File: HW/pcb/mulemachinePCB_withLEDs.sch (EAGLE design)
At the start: 31 parts, among them IC1 LD117AV50, IC2 MEGA8-P, J1 DCJ0202, Q1 16Mhz

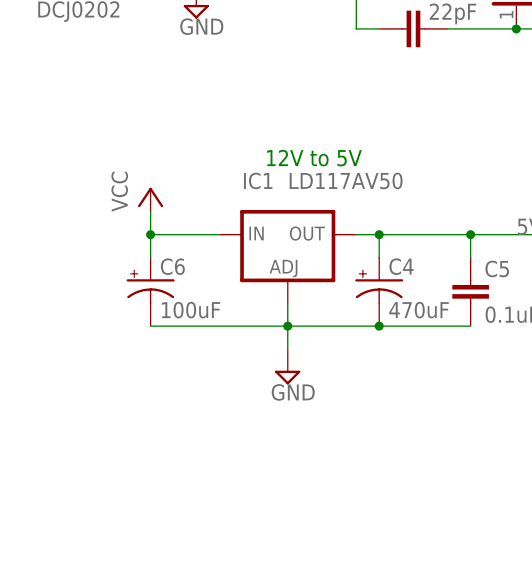
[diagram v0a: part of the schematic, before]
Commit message: changed 12V side cap C6 to 470uF. rerouted board
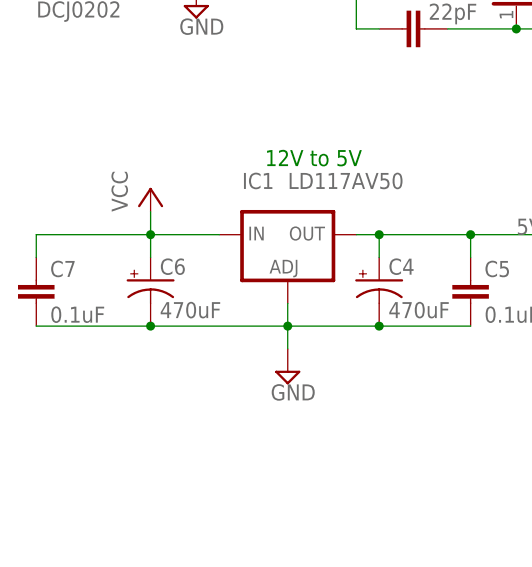
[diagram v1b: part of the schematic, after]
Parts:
- added C7: 0.1uF, capacitor-wima:C2,5-3
- C6: value 100uF -> 470uF
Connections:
- net GND: now also C7.2
- net VCC: now also C7.1
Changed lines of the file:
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@@
 <part name="T3" library="transistor-neu-to92" library_urn="urn:adsk.eagle:library:397" deviceset="*-NPN-" device="TO92-EBC" package3d_urn="urn:adsk.eagle:package:28763/2" technology="2N4401"/>
 <part name="C5" library="capacitor-wima" library_urn="urn:adsk.eagle:library:116" deviceset="C" device="2,5-3" package3d_urn="urn:adsk.eagle:package:5436/1" value="0.1uF"/>
-<part name="C6" library="rcl" library_urn="urn:adsk.eagle:library:334" deviceset="CPOL-US" device="E2.5-6" package3d_urn="urn:adsk.eagle:package:23349/1" value="100uF"/>
+<part name="C6" library="rcl" library_urn="urn:adsk.eagle:library:334" deviceset="CPOL-US" device="E2.5-6" package3d_urn="urn:adsk.eagle:package:23349/1" value="470uF"/>
 <part name="S2" library="switch-omron" library_urn="urn:adsk.eagle:library:377" deviceset="10-XX" device="" package3d_urn="urn:adsk.eagle:package:27496/1"/>
+<part name="C7" library="capacitor-wima" library_urn="urn:adsk.eagle:library:116" deviceset="C" device="2,5-3" package3d_urn="urn:adsk.eagle:package:5436/1" value="0.1uF"/>
 </parts>
 <sheets>
@@
 <attribute name="VALUE" x="71.755" y="6.35" size="1.778" layer="96"/>
 </instance>
+<instance part="C7" gate="G$1" x="-38.1" y="30.48" smashed="yes">
+<attribute name="NAME" x="-36.576" y="30.861" size="1.778" layer="95"/>
+<attribute name="VALUE" x="-36.576" y="25.781" size="1.778" layer="96"/>
+</instance>
 </instances>
 <busses>
@@
 <wire x1="-25.4" y1="33.02" x2="-25.4" y2="35.56" width="0.1524" layer="91"/>
 <junction x="-25.4" y="35.56"/>
+<wire x1="-25.4" y1="35.56" x2="-38.1" y2="35.56" width="0.1524" layer="91"/>
+<pinref part="C7" gate="G$1" pin="1"/>
+<wire x1="-38.1" y1="35.56" x2="-38.1" y2="33.02" width="0.1524" layer="91"/>
 </segment>
 <segment>
@@
 <pinref part="C6" gate="G$1" pin="-"/>
 <wire x1="-25.4" y1="25.4" x2="-10.16" y2="25.4" width="0.1524" layer="91"/>
-</segment>
-<segment>
+<pinref part="C7" gate="G$1" pin="2"/>
+<wire x1="-25.4" y1="25.4" x2="-38.1" y2="25.4" width="0.1524" layer="91"/>
+<junction x="-25.4" y="25.4"/>
+</segment>
+<segment>

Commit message: added decoupling cap for MCU to schematic. organized schematic with groups
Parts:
- added C8: 0.1uF, capacitor-wima:C2,5-3
- R1, R2, R3: value 150 -> 150R
- R4, R5, R6: value 200 -> 200R
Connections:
- net GREENLED renamed LED_GREEN
- net N$1 renamed PUMP_VODKA
- net N$22 renamed PUMP_GB
- net N$23 renamed PUMP_LIME
- net ORANGELED renamed LED_ORANGE
- net P1 renamed PUMP_VODKA_VCC
- net P2 renamed PUMP_GB_VCC
- net P3 renamed PUMP_LIME_VCC
- net YELLOWLED renamed LED_YELLOW
- net 5V: now also C8.2
- net GND: now also C8.1
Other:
- note removed: "12V to 5V"
- note removed: "DEBUG INTERFACE"
- note removed: "Manual Override Button"
- note removed: "Pump Control"
- note removed: "Strength Tuner"
- note removed: "Sweetness Tuner"
- note removed: "USER INTERFACE"
- moved on the sheet: C1, C2, C3, C4, C5, C6, C7, D1, D2, D3, IC1, IC2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

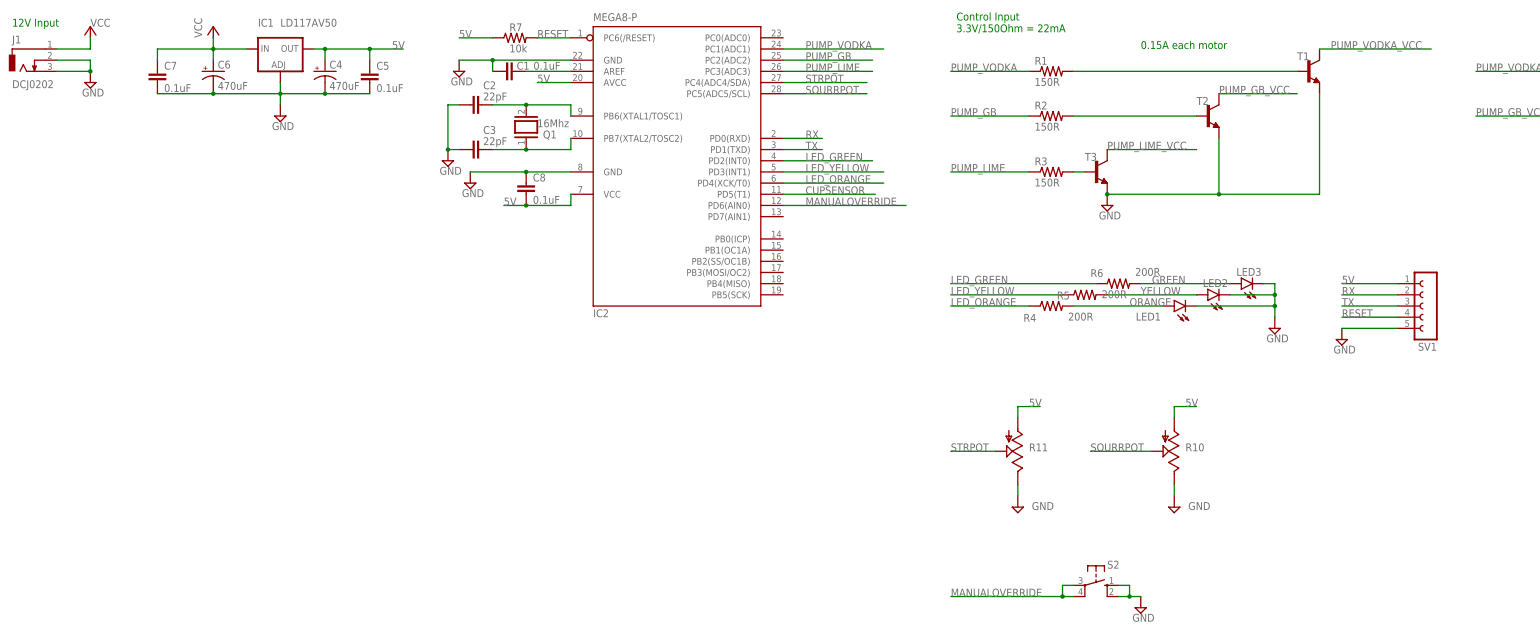
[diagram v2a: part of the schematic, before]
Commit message: rotated MCU to allow for better routing. added top and bottom layer ground planes with vias connecting them.
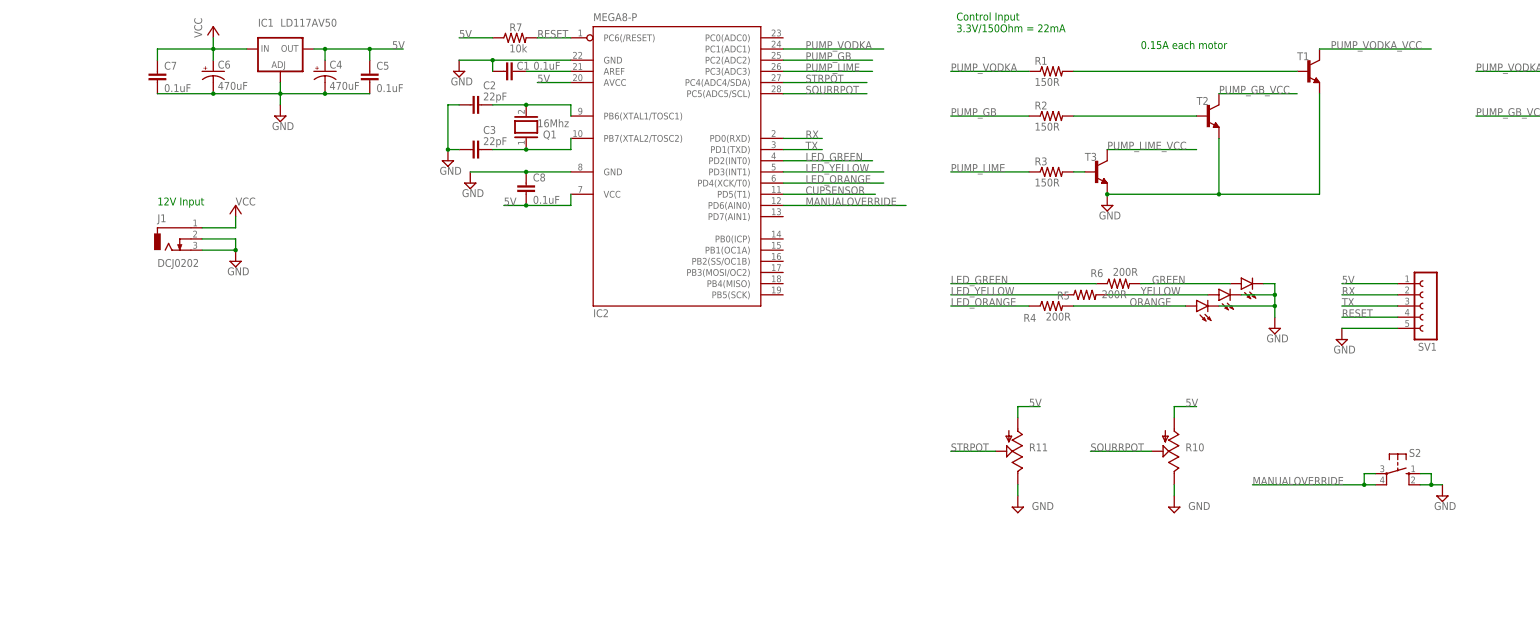
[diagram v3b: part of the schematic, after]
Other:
- moved on the sheet: J1, S2

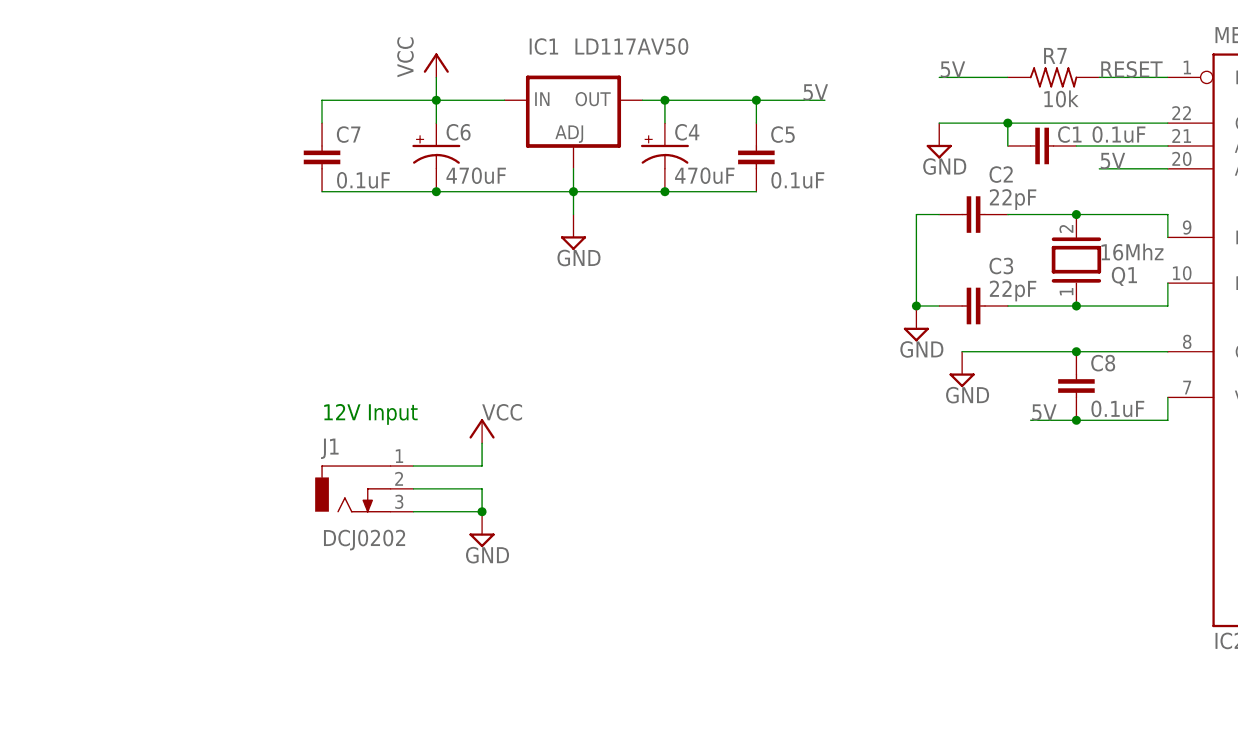
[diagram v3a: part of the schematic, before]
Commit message: adjusted net classes so that pump VCCs lines were also considered power traces (wider). rerouted and adjusted GND planes
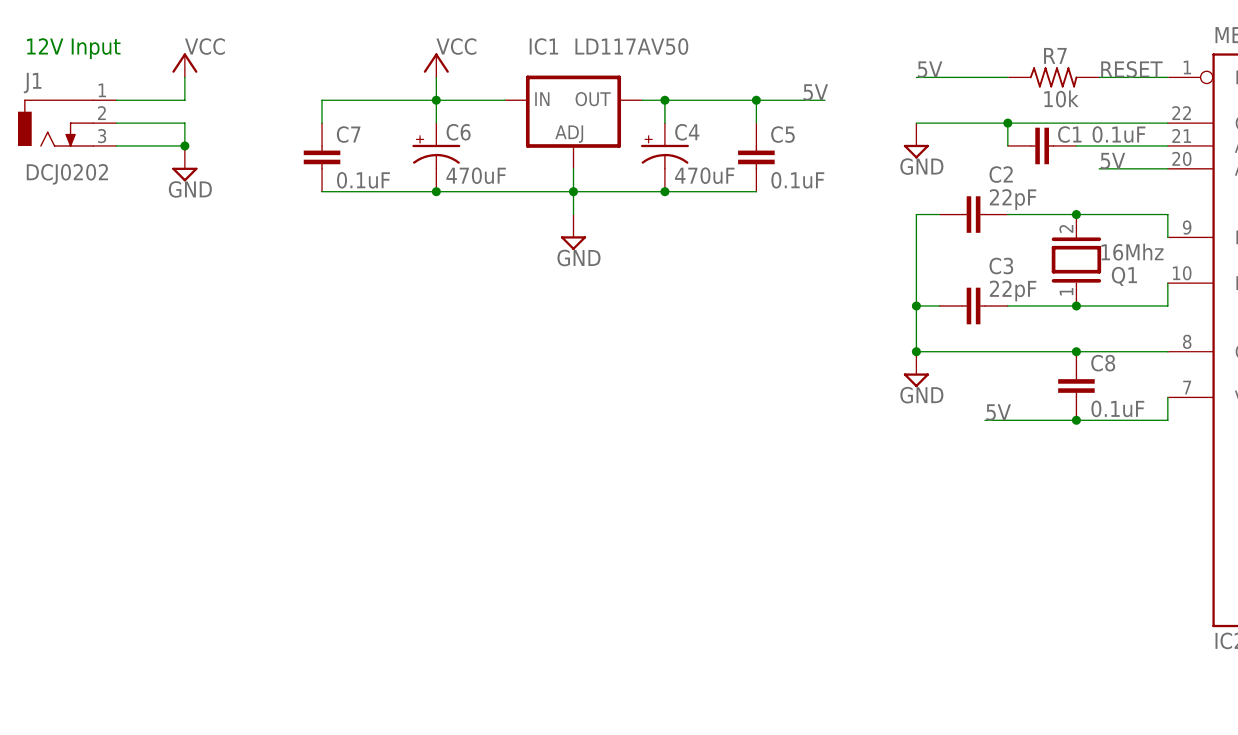
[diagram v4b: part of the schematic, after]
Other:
- moved on the sheet: J1
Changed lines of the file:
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@@
 <part name="C7" library="capacitor-wima" library_urn="urn:adsk.eagle:library:116" deviceset="C" device="2,5-3" package3d_urn="urn:adsk.eagle:package:5436/1" value="0.1uF"/>
 <part name="C8" library="capacitor-wima" library_urn="urn:adsk.eagle:library:116" deviceset="C" device="2,5-3" package3d_urn="urn:adsk.eagle:package:5436/1" value="0.1uF"/>
-<part name="SUPPLY12" library="supply2" library_urn="urn:adsk.eagle:library:372" deviceset="GND" device=""/>
 </parts>
 <sheets>
 <sheet>
 <plain>
-<text x="-68.58" y="73.66" size="1.778" layer="91" grouprefs="12VCONNECTOR">12V Input</text>
+<text x="-101.6" y="114.3" size="1.778" layer="91" grouprefs="12VCONNECTOR">12V Input</text>
 <text x="274.32" y="114.3" size="1.778" layer="91" grouprefs="PUMP_CONNECTOR">Harness</text>
 <text x="154.94" y="109.22" size="1.778" layer="91" grouprefs="PUMP_DRIVERS">0.15A each motor</text>
@@
 <attribute name="VALUE" x="-40.64" y="114.3" size="1.778" layer="96"/>
 </instance>
-<instance part="SUPPLY3" gate="GND" x="-50.8" y="60.96" smashed="yes" grouprefs="12VCONNECTOR">
-<attribute name="VALUE" x="-52.705" y="57.785" size="1.778" layer="96"/>
-</instance>
-<instance part="P+2" gate="VCC" x="-50.8" y="73.66" smashed="yes" grouprefs="12VCONNECTOR">
-<attribute name="VALUE" x="-50.8" y="73.66" size="1.778" layer="96"/>
-</instance>
-<instance part="J1" gate="G$1" x="-66.04" y="66.04" smashed="yes" grouprefs="12VCONNECTOR">
-<attribute name="NAME" x="-68.58" y="69.85" size="1.778" layer="95"/>
-<attribute name="VALUE" x="-68.58" y="59.69" size="1.778" layer="96"/>
+<instance part="SUPPLY3" gate="GND" x="-83.82" y="101.6" smashed="yes" grouprefs="12VCONNECTOR">
+<attribute name="VALUE" x="-85.725" y="98.425" size="1.778" layer="96"/>
+</instance>
+<instance part="P+2" gate="VCC" x="-83.82" y="114.3" smashed="yes" grouprefs="12VCONNECTOR">
+<attribute name="VALUE" x="-83.82" y="114.3" size="1.778" layer="96"/>
+</instance>
+<instance part="J1" gate="G$1" x="-99.06" y="106.68" smashed="yes" grouprefs="12VCONNECTOR">
+<attribute name="NAME" x="-101.6" y="110.49" size="1.778" layer="95"/>
+<attribute name="VALUE" x="-101.6" y="100.33" size="1.778" layer="96"/>
 </instance>
 <instance part="X2" gate="G$1" x="279.4" y="101.6" smashed="yes" grouprefs="PUMP_CONNECTOR">
@@
 </instance>
 <instance part="P+3" gate="VCC" x="-55.88" y="114.3" smashed="yes" grouprefs="12VTO5V">
-<attribute name="VALUE" x="-58.42" y="111.76" size="1.778" layer="96" rot="R90"/>
+<attribute name="VALUE" x="-55.88" y="114.3" size="1.778" layer="96"/>
 </instance>
 <instance part="SUPPLY6" gate="GND" x="147.32" y="73.66" smashed="yes" grouprefs="PUMP_DRIVERS">
@@
 <attribute name="VALUE" x="11.43" y="108.458" size="1.778" layer="96"/>
 </instance>
-<instance part="SUPPLY1" gate="GND" x="0" y="104.14" smashed="yes" grouprefs="MCU">
-<attribute name="VALUE" x="-1.905" y="100.965" size="1.778" layer="96"/>
+<instance part="SUPPLY1" gate="GND" x="-2.54" y="104.14" smashed="yes" grouprefs="MCU">
+<attribute name="VALUE" x="-4.445" y="100.965" size="1.778" layer="96"/>
 </instance>
 <instance part="LED1" gate="G$1" x="167.64" y="50.8" smashed="yes" rot="R90" grouprefs="USER_INTERFACE">
@@
 <attribute name="NAME" x="129.54" y="17.78" size="1.778" layer="95"/>
 </instance>
-<instance part="SUPPLY11" gate="GND" x="2.54" y="78.74" smashed="yes" grouprefs="MCU">
-<attribute name="VALUE" x="0.635" y="75.565" size="1.778" layer="96"/>
+<instance part="SUPPLY11" gate="GND" x="-2.54" y="78.74" smashed="yes" grouprefs="MCU">
+<attribute name="VALUE" x="-4.445" y="75.565" size="1.778" layer="96"/>
 </instance>
 <instance part="C1" gate="G$1" x="12.7" y="104.14" smashed="yes" rot="R270" grouprefs="MCU">
@@
 <attribute name="NAME" x="16.764" y="79.121" size="1.778" layer="95"/>
 <attribute name="VALUE" x="16.764" y="74.041" size="1.778" layer="96"/>
-</instance>
-<instance part="SUPPLY12" gate="GND" x="-2.54" y="83.82" smashed="yes" grouprefs="MCU">
-<attribute name="VALUE" x="-4.445" y="80.645" size="1.778" layer="96"/>
 </instance>
 </instances>
@@
 <pinref part="J1" gate="G$1" pin="1"/>
 <pinref part="P+2" gate="VCC" pin="VCC"/>
-<wire x1="-58.42" y1="68.58" x2="-50.8" y2="68.58" width="0.1524" layer="91" grouprefs="12VCONNECTOR"/>
-<wire x1="-50.8" y1="68.58" x2="-50.8" y2="71.12" width="0.1524" layer="91" grouprefs="12VCONNECTOR"/>
+<wire x1="-91.44" y1="109.22" x2="-83.82" y2="109.22" width="0.1524" layer="91" grouprefs="12VCONNECTOR"/>
+<wire x1="-83.82" y1="109.22" x2="-83.82" y2="111.76" width="0.1524" layer="91" grouprefs="12VCONNECTOR"/>
 </segment>
 <segment>
@@
 </segment>
 </net>
-<net name="GND" class="0">
-<segment>
-<pinref part="C2" gate="G$1" pin="2"/>
-<wire x1="-2.54" y1="96.52" x2="0" y2="96.52" width="0.1524" layer="91" grouprefs="MCU"/>
-<pinref part="C3" gate="G$1" pin="2"/>
-<wire x1="0" y1="86.36" x2="-2.54" y2="86.36" width="0.1524" layer="91" grouprefs="MCU"/>
-<wire x1="-2.54" y1="86.36" x2="-2.54" y2="96.52" width="0.1524" layer="91" grouprefs="MCU"/>
-<pinref part="SUPPLY12" gate="GND" pin="GND"/>
-<junction x="-2.54" y="86.36" grouprefs="MCU"/>
-</segment>
+<net name="GND" class="1">
 <segment>
 <pinref part="SUPPLY3" gate="GND" pin="GND"/>
 <pinref part="J1" gate="G$1" pin="2"/>
-<wire x1="-58.42" y1="66.04" x2="-50.8" y2="66.04" width="0.1524" layer="91" grouprefs="12VCONNECTOR"/>
-<wire x1="-50.8" y1="66.04" x2="-50.8" y2="63.5" width="0.1524" layer="91" grouprefs="12VCONNECTOR"/>
-<junction x="-50.8" y="63.5" grouprefs="12VCONNECTOR"/>
+<wire x1="-91.44" y1="106.68" x2="-83.82" y2="106.68" width="0.1524" layer="91" grouprefs="12VCONNECTOR"/>
+<wire x1="-83.82" y1="106.68" x2="-83.82" y2="104.14" width="0.1524" layer="91" grouprefs="12VCONNECTOR"/>
+<junction x="-83.82" y="104.14" grouprefs="12VCONNECTOR"/>
 <pinref part="J1" gate="G$1" pin="3"/>
-<wire x1="-58.42" y1="63.5" x2="-50.8" y2="63.5" width="0.1524" layer="91" grouprefs="12VCONNECTOR"/>
+<wire x1="-91.44" y1="104.14" x2="-83.82" y2="104.14" width="0.1524" layer="91" grouprefs="12VCONNECTOR"/>
 </segment>
 <segment>
@@
 <segment>
 <pinref part="IC2" gate="G$1" pin="GND"/>
-<wire x1="0" y1="106.68" x2="7.62" y2="106.68" width="0.1524" layer="91" grouprefs="MCU"/>
+<wire x1="-2.54" y1="106.68" x2="7.62" y2="106.68" width="0.1524" layer="91" grouprefs="MCU"/>
 <pinref part="SUPPLY1" gate="GND" pin="GND"/>
 <pinref part="C1" gate="G$1" pin="2"/>
@@
 <pinref part="SUPPLY11" gate="GND" pin="GND"/>
 <pinref part="IC2" gate="G$1" pin="GND@1"/>
-<wire x1="2.54" y1="81.28" x2="15.24" y2="81.28" width="0.1524" layer="91" grouprefs="MCU"/>
+<wire x1="-2.54" y1="81.28" x2="15.24" y2="81.28" width="0.1524" layer="91" grouprefs="MCU"/>
 <pinref part="C8" gate="G$1" pin="1"/>
 <wire x1="15.24" y1="81.28" x2="25.4" y2="81.28" width="0.1524" layer="91" grouprefs="MCU"/>
 <junction x="15.24" y="81.28" grouprefs="MCU"/>
+<pinref part="C2" gate="G$1" pin="2"/>
+<wire x1="-2.54" y1="96.52" x2="0" y2="96.52" width="0.1524" layer="91" grouprefs="MCU"/>
+<pinref part="C3" gate="G$1" pin="2"/>
+<wire x1="0" y1="86.36" x2="-2.54" y2="86.36" width="0.1524" layer="91" grouprefs="MCU"/>
+<wire x1="-2.54" y1="86.36" x2="-2.54" y2="96.52" width="0.1524" layer="91" grouprefs="MCU"/>
+<wire x1="-2.54" y1="86.36" x2="-2.54" y2="81.28" width="0.1524" layer="91"/>
+<junction x="-2.54" y="86.36"/>
+<junction x="-2.54" y="81.28"/>
 </segment>
 <segment>
@@
 <segment>
 <pinref part="R7" gate="G$1" pin="1"/>
-<wire x1="7.62" y1="111.76" x2="0" y2="111.76" width="0.1524" layer="91" grouprefs="MCU"/>
-<label x="0" y="111.76" size="1.778" layer="95" grouprefs="MCU"/>
+<wire x1="7.62" y1="111.76" x2="-2.54" y2="111.76" width="0.1524" layer="91" grouprefs="MCU"/>
+<label x="-2.54" y="111.76" size="1.778" layer="95" grouprefs="MCU"/>
 </segment>
 <segment>
@@
 <wire x1="15.24" y1="73.66" x2="25.4" y2="73.66" width="0.1524" layer="91" grouprefs="MCU"/>
 <wire x1="25.4" y1="73.66" x2="25.4" y2="76.2" width="0.1524" layer="91" grouprefs="MCU"/>
-<wire x1="15.24" y1="73.66" x2="10.16" y2="73.66" width="0.1524" layer="91" grouprefs="MCU"/>
+<wire x1="15.24" y1="73.66" x2="5.08" y2="73.66" width="0.1524" layer="91" grouprefs="MCU"/>
 <junction x="15.24" y="73.66" grouprefs="MCU"/>
-<label x="10.16" y="73.66" size="1.778" layer="95" grouprefs="MCU"/>
+<label x="5.08" y="73.66" size="1.778" layer="95" grouprefs="MCU"/>
 </segment>
 </net>
